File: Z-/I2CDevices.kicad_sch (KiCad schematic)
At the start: 36 parts, among them U1 OPT4003DNPRQ1, U2 LTC4316xDD, U3 ADM1176-1ARMZ-R7, U4 NCV891330PD50R2G, U5 DRV8830DRC

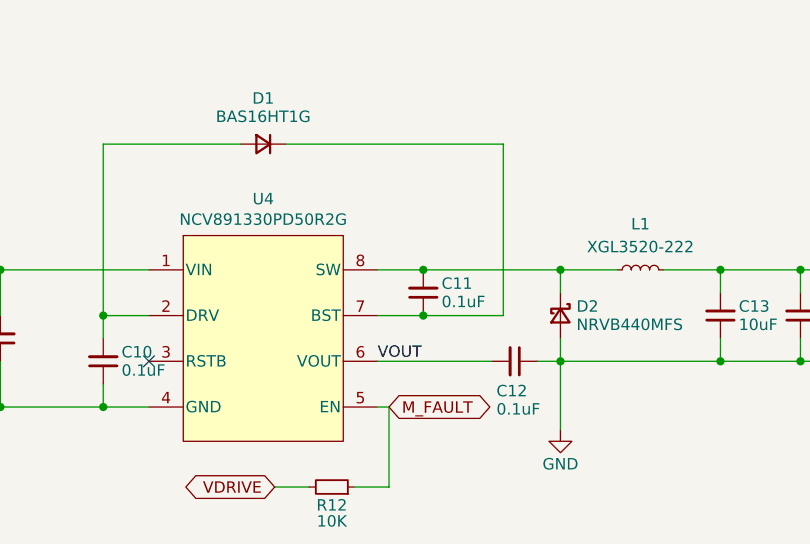
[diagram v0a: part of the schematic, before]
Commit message: Reworked board layout
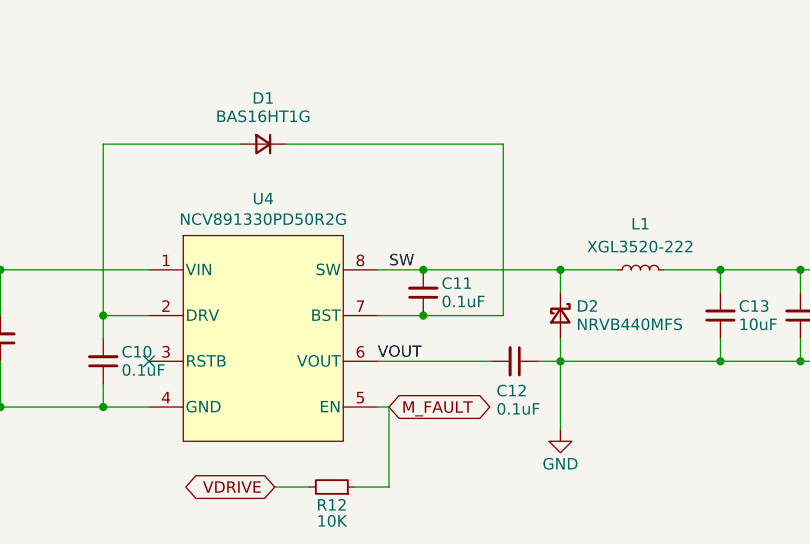
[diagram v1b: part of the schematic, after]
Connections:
- net SW: now reaches C11.2, D2.1 (K), L1.1, U4.8 (SW)
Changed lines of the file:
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@@
+		)
+	)
+	(label "SW"
+		(at 209.55 57.15 0)
+		(fields_autoplaced yes)
+		(effects
+			(font
+				(size 1.27 1.27)
+			)
+			(justify left bottom)
 		)
 	)

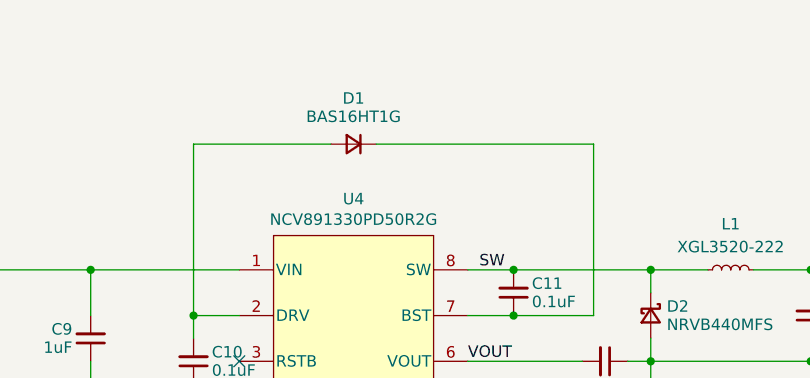
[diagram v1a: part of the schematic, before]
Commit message: First pass on routing and silkscreen
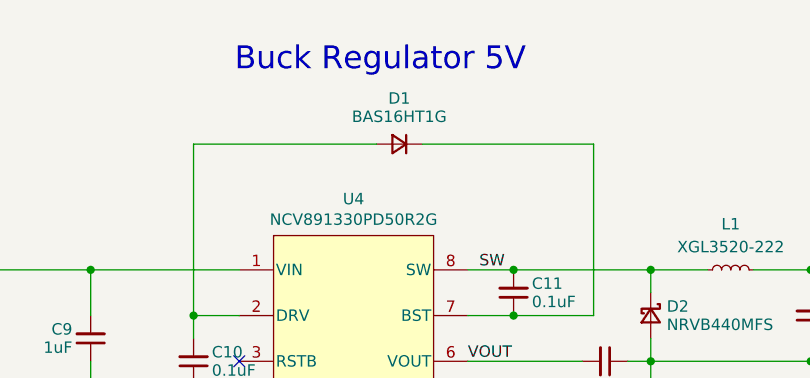
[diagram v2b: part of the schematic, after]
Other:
- note added: "Buck Regulator 5V"
- moved on the sheet: D1
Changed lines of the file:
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@@
 	(wire
 		(pts
-			(xy 198.12 43.18) (xy 222.25 43.18)
+			(xy 203.2 43.18) (xy 222.25 43.18)
 		)
 		(stroke
@@
 	(wire
 		(pts
-			(xy 177.8 43.18) (xy 193.04 43.18)
+			(xy 177.8 43.18) (xy 198.12 43.18)
 		)
 		(stroke
@@
 		)
 	)
+	(text "Buck Regulator 5V"
+		(exclude_from_sim no)
+		(at 182.372 35.306 0)
+		(effects
+			(font
+				(size 2.54 2.54)
+			)
+			(justify left bottom)
+		)
+	)
 	(label "SCLOUT"
 		(at 99.06 97.79 0)
@@
 	(symbol
 		(lib_id "SolarPanels:D_Small")
-		(at 195.58 43.18 180)
+		(at 200.66 43.18 180)
 		(unit 1)
 		(exclude_from_sim no)
@@
 		(dnp no)
 		(property "Reference" "D1"
-			(at 195.58 38.1 0)
+			(at 200.66 38.1 0)
 			(effects
 				(font
@@
 		)
 		(property "Value" "BAS16HT1G"
-			(at 195.58 40.132 0)
+			(at 200.66 40.132 0)
 			(effects
 				(font
@@
 		)
 		(property "Footprint" "Diode_SMD:D_SOD-323"
-			(at 195.58 43.18 90)
+			(at 200.66 43.18 90)
 			(effects
 				(font
@@
 		)
 		(property "Datasheet" "~"
-			(at 195.58 43.18 90)
+			(at 200.66 43.18 90)
 			(effects
 				(font
@@
 		)
 		(property "Description" "Diode, small symbol"
-			(at 195.58 43.18 0)
+			(at 200.66 43.18 0)
 			(effects
 				(font
@@
 		)
 		(property "Sim.Device" "D"
-			(at 195.58 43.18 0)
+			(at 200.66 43.18 0)
 			(effects
 				(font
@@
 		)
 		(property "Sim.Pins" "1=K 2=A"
-			(at 195.58 43.18 0)
+			(at 200.66 43.18 0)
 			(effects
 				(font

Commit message: Stuff idk
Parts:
- added R69, R70: 0R (DNI), Resistor_SMD:R_0603_1608Metric, symbol SolarPanels:R_Small
- added R71, R72: 0R, Resistor_SMD:R_0402_1005Metric, symbol SolarPanels:R_Small
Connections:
- net SCLOUT: now also R69.2, R72.1
- net SCL_LS: now also R69.1
- net SDAOUT: now also R70.2, R71.2
- net SDA_LS: now also R70.1
- net ADDR: now reaches R25.1, R26.2, U1.2 (ADDR)
- net ADDR: now also R71.1, R72.2
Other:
- note added: "I2C ADDR Install R25: 0x45 Install R26: 0x44"
- note removed: "I2C ADDR Install R34: 0x45 Install R35: 0x44"

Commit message: Review fixes
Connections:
- net VBATT renamed VBATT_SENSE
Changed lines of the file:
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@@
 		)
 	)
-	(global_label "VBATT"
+	(global_label "VBATT_SENSE"
 		(shape bidirectional)
 		(at 44.45 151.13 180)
